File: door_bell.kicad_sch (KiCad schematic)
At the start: 75 parts, among them J1 8-10V AC/DC, J2 Speaker, J3 SWITCH1, J4 Door panel, J5 UART, J6 JTAG, J7 BOOT, J8 MicroSD, K1 HJR 1-2C, Q1 BC847, SW1 Reset, U1 NCP1117-5v, U2 MAX98357A, U3 NCP1117-3v3, U4 DS3231M, U5 MAX3232, U6 ESP32-WROVER-B, U7 74LVC2G14

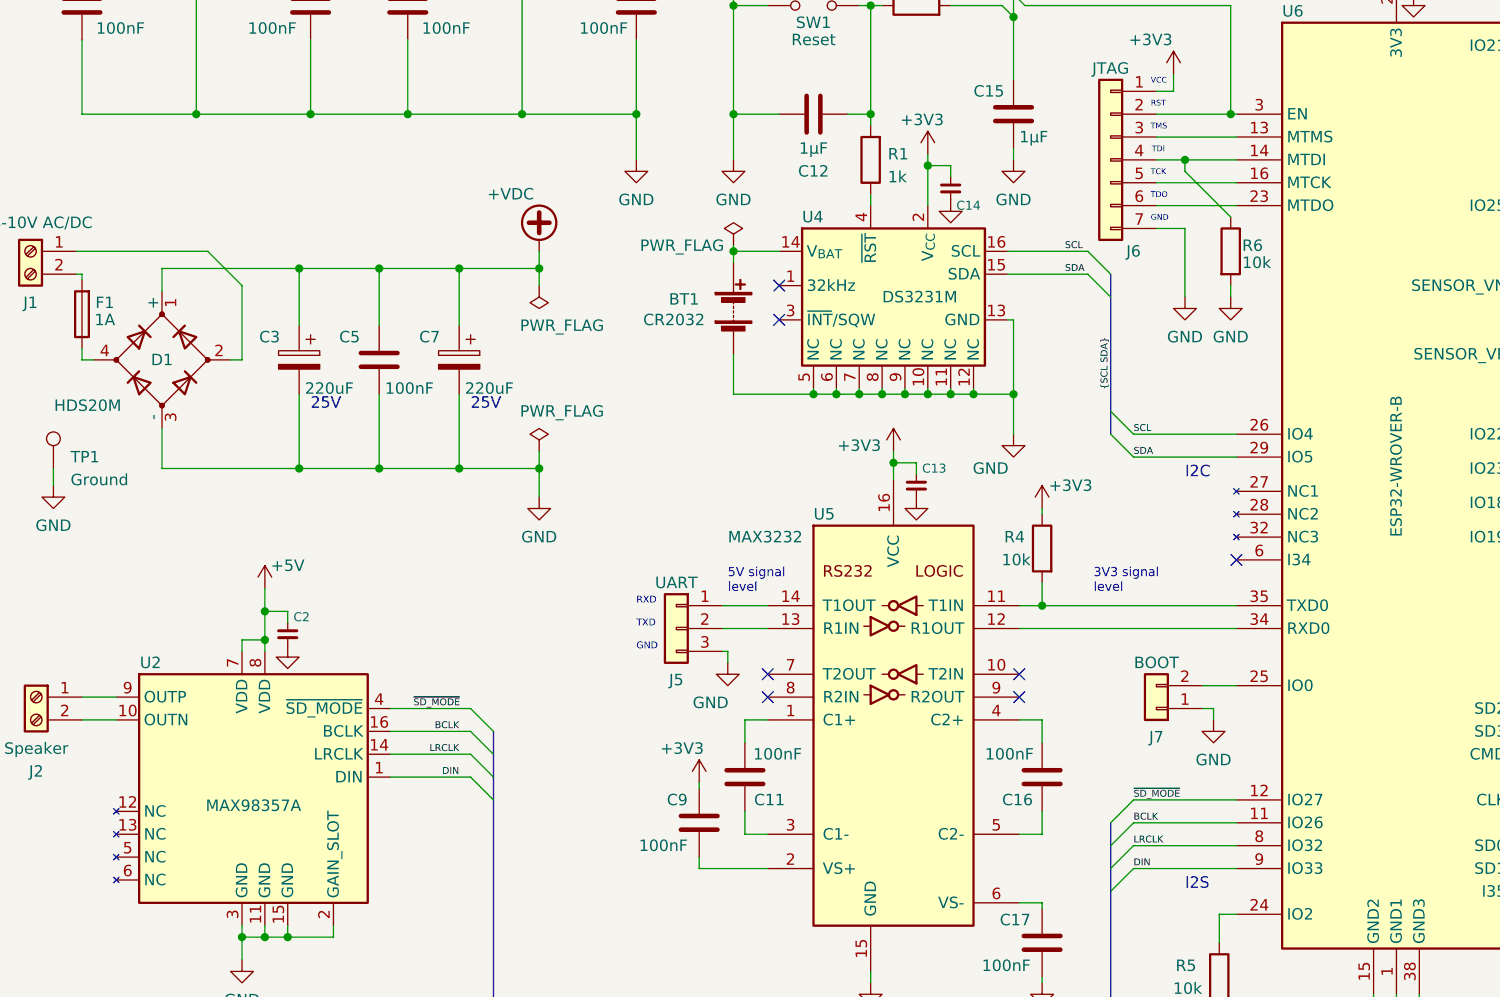
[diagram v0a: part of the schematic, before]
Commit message: Redraw, v.1.1 - fix errors
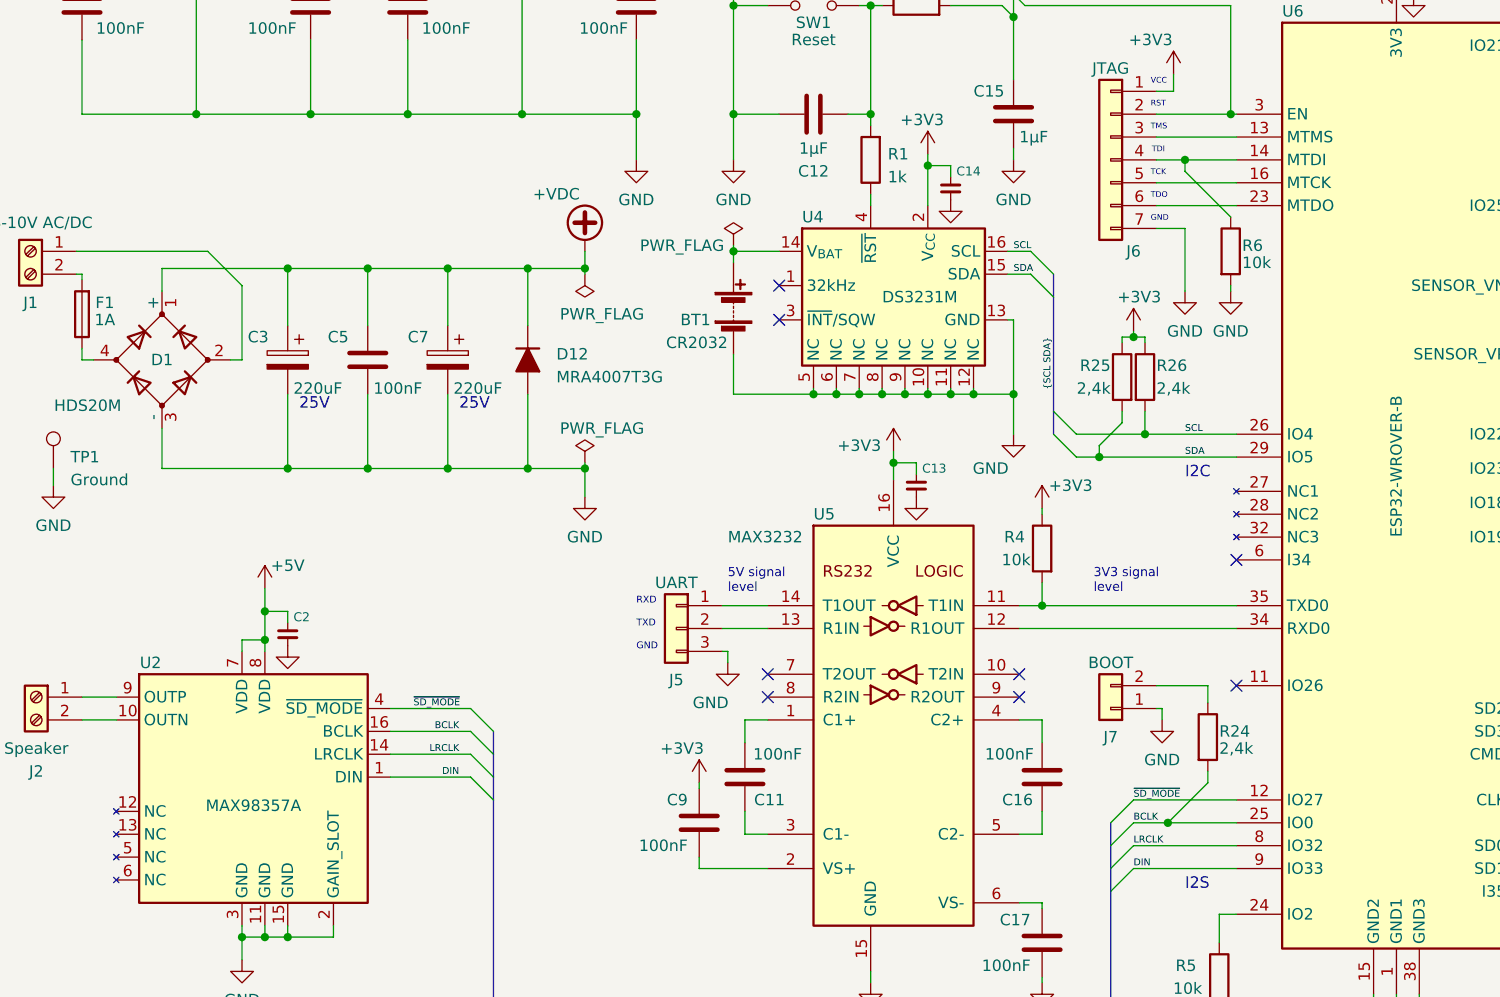
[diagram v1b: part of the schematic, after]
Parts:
- added D12: MRA4007T3G, Diode_SMD:D_SMB_Handsoldering, symbol Device:D_Filled
- added R24, R25, R26: 2,4k, Resistor_SMD:R_0805_2012Metric_Pad1.20x1.40mm_HandSolder, symbol Device:R
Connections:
- net +3V3: now also R25.1, R26.1
- net +VDC: now also D12.1 (K)
- net BCLK: now also U6.25 (IO0), R24.2; no longer U6.11 (IO26)
- net GND: now also D12.2 (A)
- net SCL: now also R26.2
- net SDA: now also R25.2
- net at J7.2 (Pin_2): now also R24.1; no longer U6.25 (IO0)
- no-connect marks 10 -> 11
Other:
- moved on the sheet: C3, C5, C7, J7

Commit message: Reallocate pads for LEDS and Panel buttons
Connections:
- net at R9.1: now also U6.10 (IO25); no longer U6.4 (SENSOR_VP)
- net at U7.4: now also U6.4 (SENSOR_VP); no longer U6.10 (IO25)
- net at U6.33 (IO21): now also R8.1; no longer U7.6
- net at U6.5 (SENSOR_VN): now also U7.6; no longer R8.1

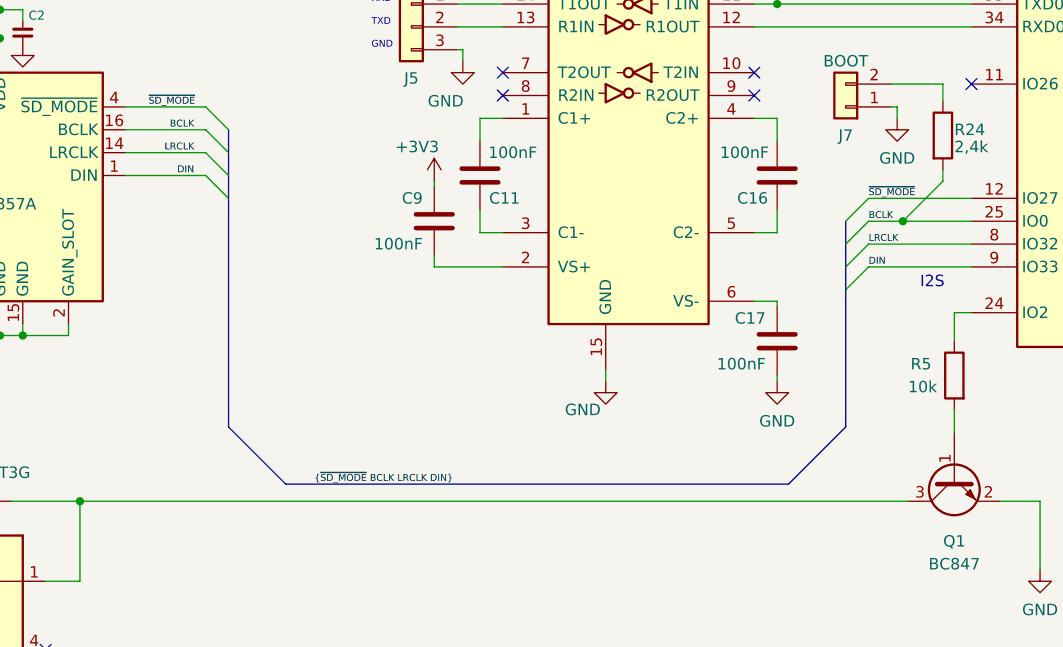
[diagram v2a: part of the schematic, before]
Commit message: Swap to C++, begin app structuring
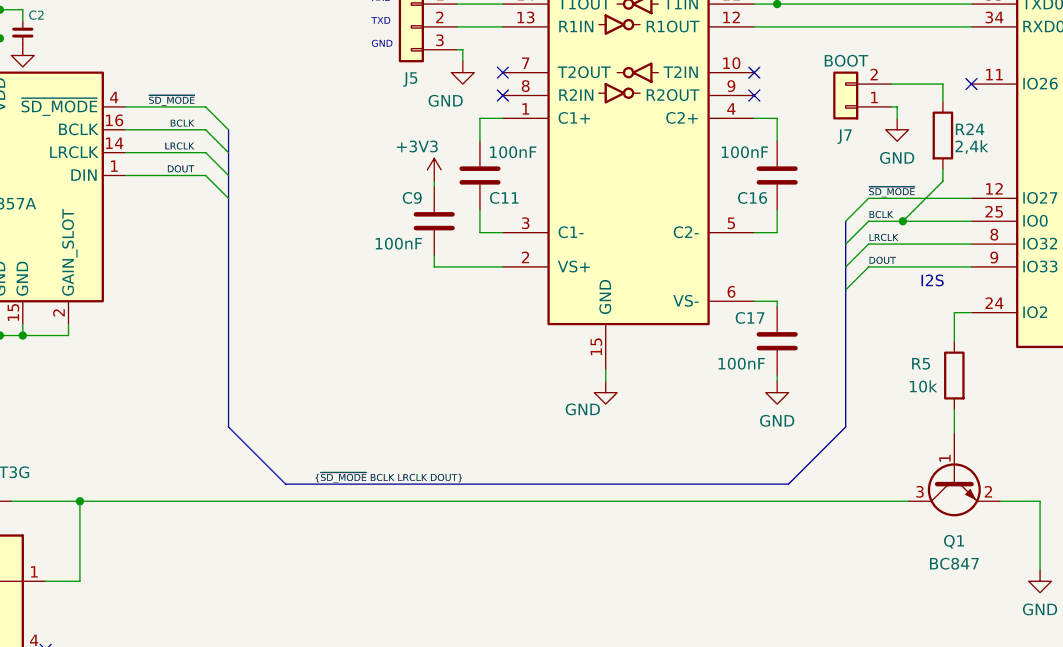
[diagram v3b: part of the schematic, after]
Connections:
- net DIN renamed DOUT
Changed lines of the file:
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@@
     (effects (font (size 0.762 0.762)) (justify right bottom))
   )
-  (label "DIN" (at 72.39 124.46 180) (fields_autoplaced)
+  (label "DOUT" (at 72.39 124.46 180) (fields_autoplaced)
     (effects (font (size 0.762 0.762)) (justify right bottom))
   )
@@
     (effects (font (size 0.762 0.762)) (justify left bottom))
   )
-  (label "DIN" (at 147.32 134.62 0) (fields_autoplaced)
+  (label "DOUT" (at 147.32 134.62 0) (fields_autoplaced)
     (effects (font (size 0.762 0.762)) (justify left bottom))
   )
@@
     (effects (font (size 0.762 0.762)) (justify left bottom))
   )
-  (label "{~{SD_MODE} BCLK LRCLK DIN}" (at 85.725 158.75 0) (fields_autoplaced)
+  (label "{~{SD_MODE} BCLK LRCLK DOUT}" (at 85.725 158.75 0) (fields_autoplaced)
     (effects (font (size 0.762 0.762)) (justify left bottom))
   )

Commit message: Update schematics, fix problems
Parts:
- removed J6: JTAG, Connector_PinHeader_1.27mm:PinHeader_1x07_P1.27mm_Vertical, symbol Connector_Generic:Conn_01x07
- removed J7: BOOT, Connector_PinHeader_1.27mm:PinHeader_1x02_P1.27mm_Vertical, symbol Connector_Generic:Conn_01x02
- removed TP1: Ground, TestPoint:TestPoint_Loop_D3.50mm_Drill0.9mm_Beaded, symbol Connector:TestPoint
- added SW2: Boot, Button_Switch_SMD_espena:SW_SPST_TL3301_6x6mm_H4.3mm, symbol Switch:SW_Push
- C3, C7: footprint Capacitor_SMD:C_Elec_8x10.2 -> Capacitor_SMD:CP_Elec_6.3x9.9
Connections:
- net GND: now also SW2.1
- net SPICS: now reaches D10.2 (A2), J8.2 (DAT3/CD), R18.2
- net SPICS: now also U6.11 (IO26); no longer U6.18 (SD3)
- net SPIMOSI: now reaches D9.2 (A2), J8.3 (CMD), R17.2
- net SPIMOSI: now also U6.13 (IO14); no longer U6.19 (CMD)
- net at D4.2 (A2), J8.8 (DAT1), R10.2: no longer U6.22 (SD1)
- net at D11.2 (A2), J8.1 (DAT2), R19.2: no longer U6.17 (SD2)
- net SPICLK: now reaches D8.2 (A2), J8.5 (CLK), R16.2
- net SPICLK: now also U6.23 (IO15); no longer U6.20 (CLK)
- net SPIMISO: now reaches D5.2 (A2), J8.7 (DAT0), R15.2
- net SPIMISO: now also U6.16 (IO13); no longer U6.21 (SD0)
- net at R24.1: now also SW2.2
- no-connect marks 11 -> 17
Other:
- note removed: "RST"
- note removed: "TCK"
- note removed: "TDI"
- note removed: "TDO"
- note removed: "TMS"
- note removed: "VCC"
- moved on the sheet: Q1, R24, R6

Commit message: Replace TVS diodes with larger type (SOD-923 -> SOD-523)
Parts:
- D10, D11, D3, D4, D5, D8, D9: footprint Diode_SMD:D_SOD-923 -> Diode_SMD:D_SOD-523
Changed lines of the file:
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@@
       (effects (font (size 1.27 1.27)) (justify right))
     )
-    (property "Footprint" "Diode_SMD:D_SOD-923" (at 196.85 144.145 0)
+    (property "Footprint" "Diode_SMD:D_SOD-523" (at 196.85 144.145 0)
       (effects (font (size 1.27 1.27)) hide)
     )
@@
       (effects (font (size 1.27 1.27)) (justify right))
     )
-    (property "Footprint" "Diode_SMD:D_SOD-923" (at 222.25 144.145 0)
+    (property "Footprint" "Diode_SMD:D_SOD-523" (at 222.25 144.145 0)
       (effects (font (size 1.27 1.27)) hide)
     )
@@
       (effects (font (size 1.27 1.27)) (justify right))
     )
-    (property "Footprint" "Diode_SMD:D_SOD-923" (at 201.93 144.145 0)
+    (property "Footprint" "Diode_SMD:D_SOD-523" (at 201.93 144.145 0)
       (effects (font (size 1.27 1.27)) hide)
     )
@@
       (effects (font (size 1.27 1.27)) (justify right))
     )
-    (property "Footprint" "Diode_SMD:D_SOD-923" (at 227.33 144.145 0)
+    (property "Footprint" "Diode_SMD:D_SOD-523" (at 227.33 144.145 0)
       (effects (font (size 1.27 1.27)) hide)
     )
@@
       (effects (font (size 1.27 1.27)) (justify right))
     )
-    (property "Footprint" "Diode_SMD:D_SOD-923" (at 217.17 144.145 0)
+    (property "Footprint" "Diode_SMD:D_SOD-523" (at 217.17 144.145 0)
       (effects (font (size 1.27 1.27)) hide)
     )
@@
       (effects (font (size 1.27 1.27)) (justify right))
     )
-    (property "Footprint" "Diode_SMD:D_SOD-923" (at 212.09 144.145 0)
+    (property "Footprint" "Diode_SMD:D_SOD-523" (at 212.09 144.145 0)
       (effects (font (size 1.27 1.27)) hide)
     )
@@
       (effects (font (size 1.27 1.27)) (justify right))
     )
-    (property "Footprint" "Diode_SMD:D_SOD-923" (at 207.01 144.145 0)
-      (effects (font (size 1.27 1.27)) hide)
-    )
+    (property "Footprint" "Diode_SMD:D_SOD-523" (at 207.01 144.145 0)
+      (effects (font (size 1.27 1.27)) hide)
+    )
